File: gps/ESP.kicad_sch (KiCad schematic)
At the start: 23 parts, among them J12 ENC+RGB, J13 ENC+RGB, J7 USB_B_Micro, J9 USB_pads, SW1 RotaryEncoder_Switch, U11 SN74LV1T34DBVRG4, U3 DFR0654, U9 TCA39306DDFR

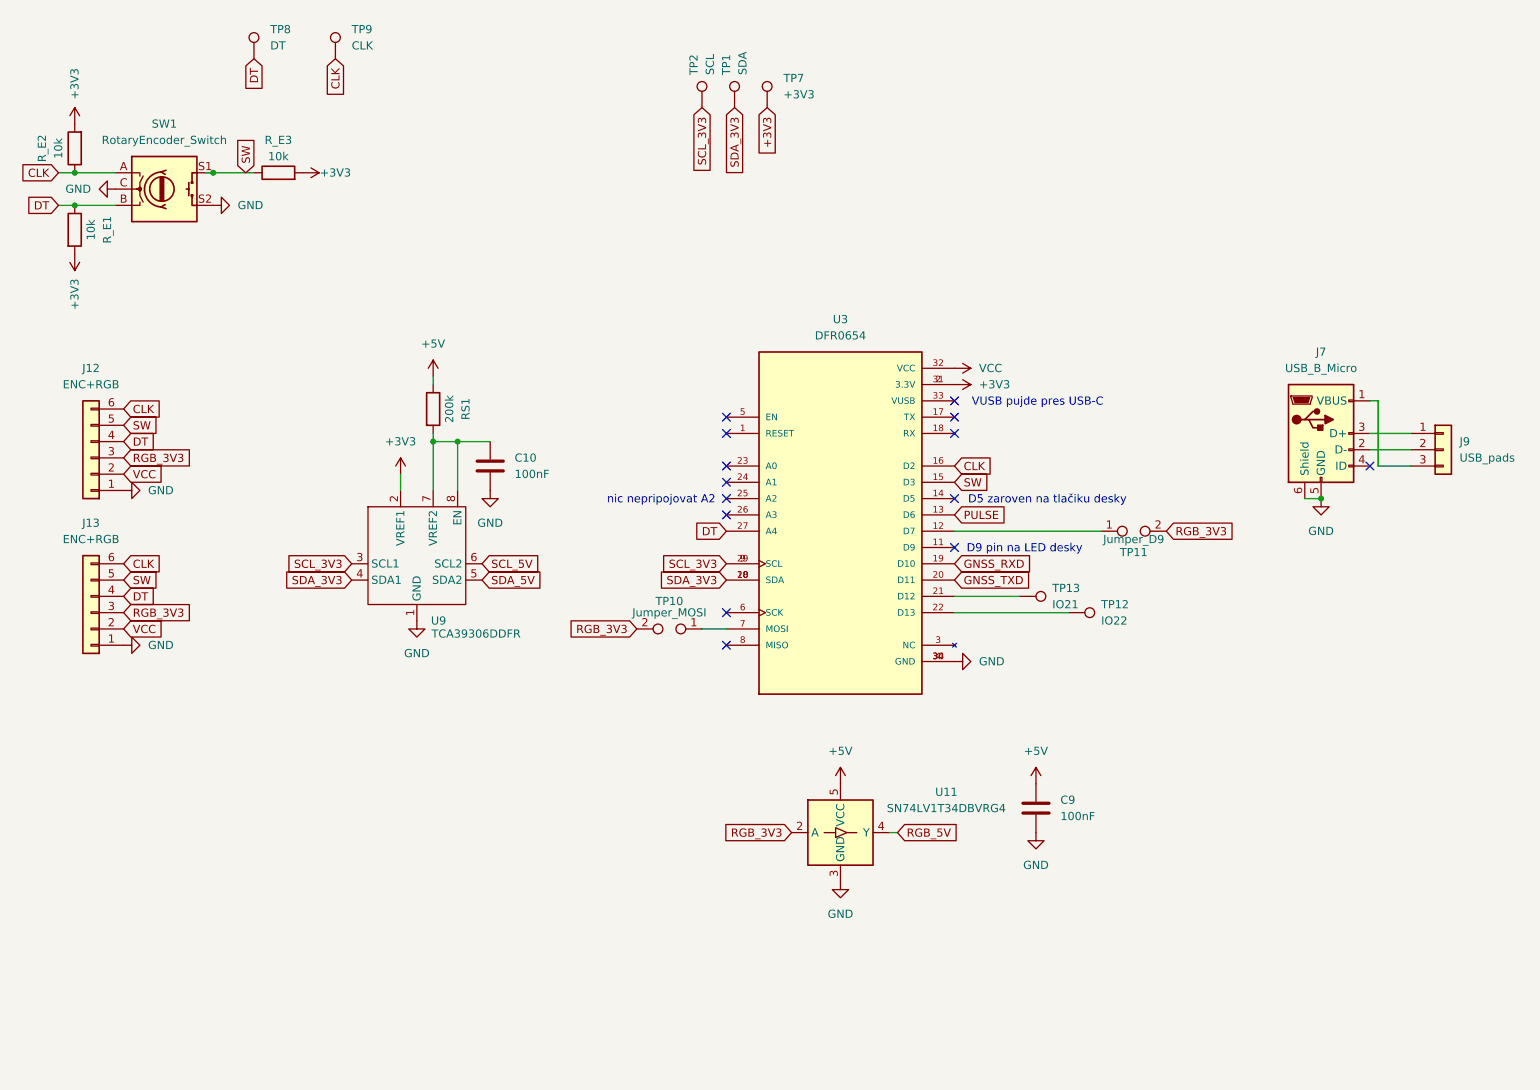
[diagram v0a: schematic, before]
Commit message: added pullup for 3V3 i2c
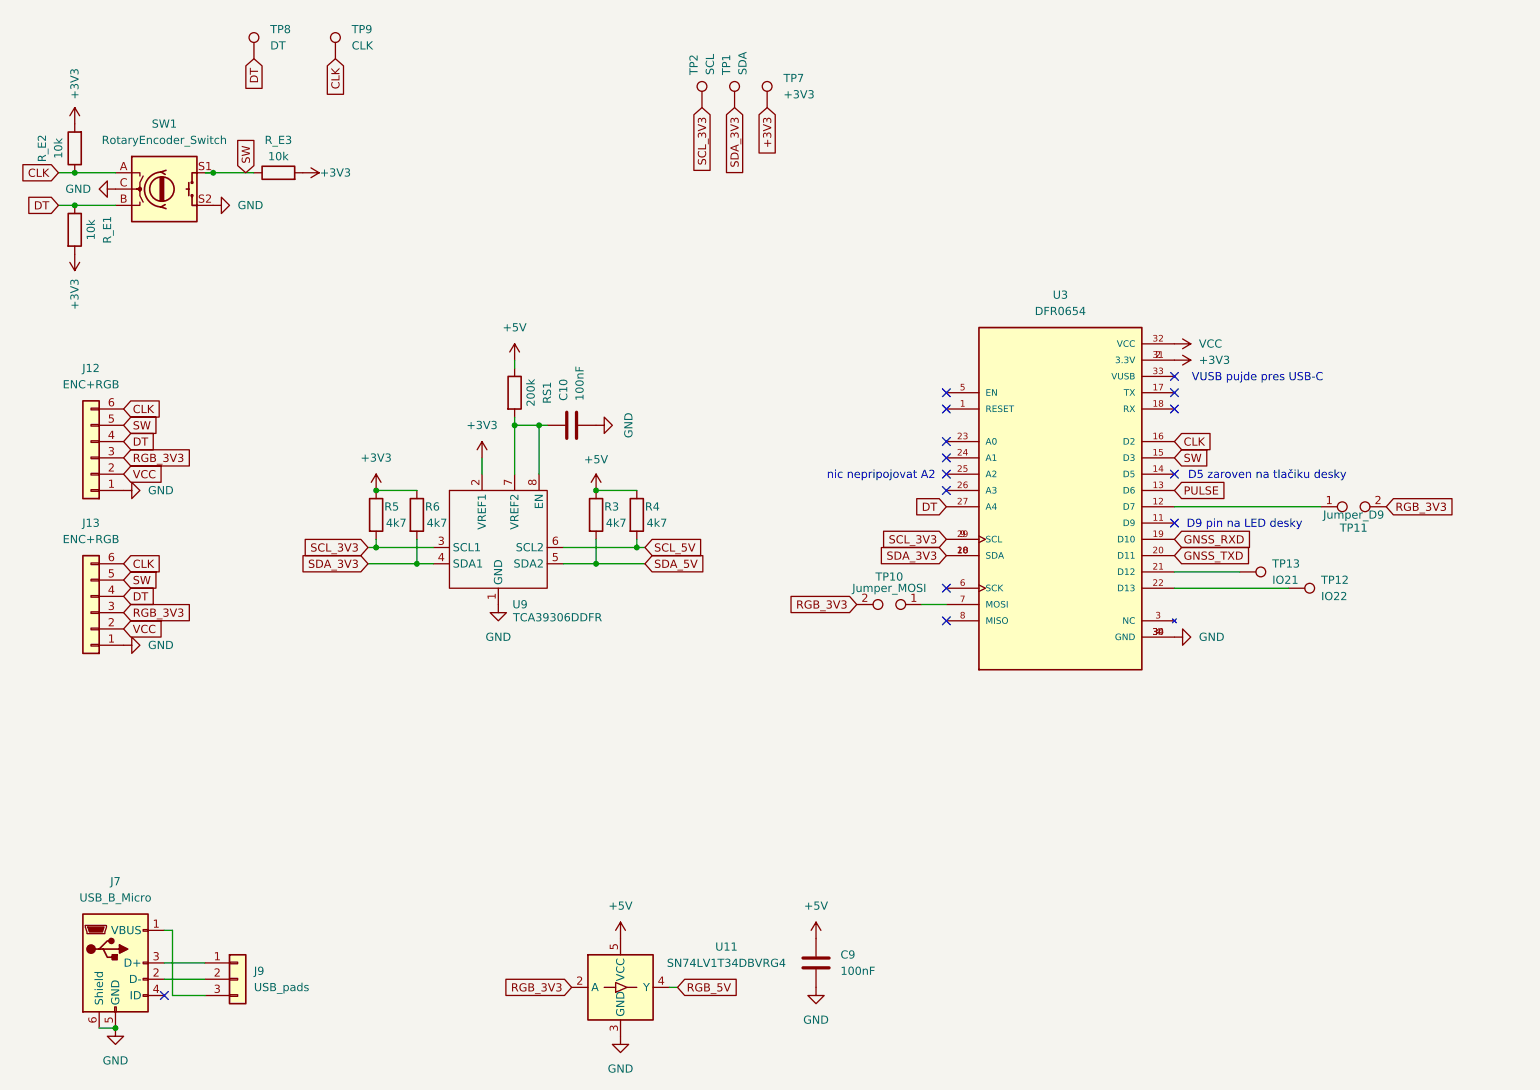
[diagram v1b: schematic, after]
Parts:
- added R3, R4, R5, R6: 4k7, Resistor_SMD:R_0805_2012Metric_Pad1.20x1.40mm_HandSolder, symbol Device:R
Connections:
- net +3V3: now also R5.1, R6.1
- net +5V: now also R3.1, R4.1
- net SCL_3V3: now also R5.2
- net SCL_5V: now also R4.2
- net SDA_3V3: now also R6.2
- net SDA_5V: now also R3.2
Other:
- moved on the sheet: C10, C9, J7, J9, RS1, TP10, TP11, TP12, TP13, U11, U3, U9

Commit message: added gerbers
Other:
- moved on the sheet: C10, R_E3, TP8, TP9
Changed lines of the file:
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@@
 	)
 	(junction
-		(at 55.88 43.18)
-		(diameter 0)
-		(color 0 0 0 0)
-	)
-	(junction
 		(at 121.92 101.6)
 		(diameter 0)
@@
 		(color 0 0 0 0)
 	)
+	(junction
+		(at 64.77 43.18)
+		(diameter 0)
+		(color 0 0 0 0)
+	)
 	(no_connect
 		(at 205.74 90.17)
@@
 	(wire
 		(pts
-			(xy 87.63 100.33) (xy 87.63 104.14)
+			(xy 67.31 43.18) (xy 64.77 43.18)
 		)
 		(stroke
@@
 	(wire
 		(pts
-			(xy 102.87 82.55) (xy 102.87 90.17)
+			(xy 87.63 100.33) (xy 87.63 104.14)
 		)
 		(stroke
@@
 	(wire
 		(pts
-			(xy 54.61 43.18) (xy 55.88 43.18)
+			(xy 102.87 82.55) (xy 102.87 90.17)
 		)
 		(stroke
@@
 	(wire
 		(pts
-			(xy 107.95 82.55) (xy 106.68 82.55)
+			(xy 110.49 82.55) (xy 106.68 82.55)
 		)
 		(stroke
@@
 	(wire
 		(pts
-			(xy 55.88 43.18) (xy 62.23 43.18)
-		)
-		(stroke
-			(width 0)
-			(type default)
-		)
-	)
-	(wire
-		(pts
 			(xy 80.01 104.14) (xy 87.63 104.14)
 		)
@@
 	(wire
 		(pts
+			(xy 64.77 43.18) (xy 55.88 43.18)
+		)
+		(stroke
+			(width 0)
+			(type default)
+		)
+	)
+	(wire
+		(pts
 			(xy 34.29 43.18) (xy 40.64 43.18)
 		)
@@
 	(global_label "DT"
 		(shape input)
-		(at 62.23 25.4 270)
+		(at 73.66 24.13 270)
 		(fields_autoplaced yes)
 		(effects
@@
 		)
 		(property "Intersheetrefs" "${INTERSHEET_REFS}"
-			(at 62.23 30.6228 90)
+			(at 73.66 29.3528 90)
 			(effects
 				(font
@@
 	(global_label "SW"
 		(shape input)
-		(at 60.96 43.18 90)
+		(at 67.31 43.18 0)
 		(fields_autoplaced yes)
 		(effects
@@
 		)
 		(property "Intersheetrefs" "${INTERSHEET_REFS}"
-			(at 60.96 37.5339 90)
+			(at 72.9561 43.18 0)
 			(effects
 				(font
@@
 	(global_label "CLK"
 		(shape input)
-		(at 74.93 25.4 270)
+		(at 86.36 24.13 270)
 		(fields_autoplaced yes)
 		(effects
@@
 		)
 		(property "Intersheetrefs" "${INTERSHEET_REFS}"
-			(at 74.93 31.9533 90)
+			(at 86.36 30.6833 90)
 			(effects
 				(font
@@
 	(symbol
 		(lib_id "Device:C")
-		(at 111.76 82.55 270)
+		(at 114.3 82.55 270)
 		(unit 1)
 		(exclude_from_sim no)
@@
 		(fields_autoplaced yes)
 		(property "Reference" "C10"
-			(at 110.4899 78.74 0)
+			(at 113.0299 78.74 0)
 			(effects
 				(font
@@
 		)
 		(property "Value" "100nF"
-			(at 113.0299 78.74 0)
+			(at 115.5699 78.74 0)
 			(effects
 				(font
@@
 		)
 		(property "Footprint" "Capacitor_SMD:C_0805_2012Metric_Pad1.18x1.45mm_HandSolder"
-			(at 107.95 83.5152 0)
+			(at 110.49 83.5152 0)
 			(effects
 				(font
@@
 		)
 		(property "Datasheet" "~"
-			(at 111.76 82.55 0)
+			(at 114.3 82.55 0)
 			(effects
 				(font
@@
 		)
 		(property "Description" "Unpolarized capacitor"
-			(at 111.76 82.55 0)
+			(at 114.3 82.55 0)
 			(effects
 				(font
@@
 	(symbol
 		(lib_id "Device:R")
-		(at 66.04 43.18 90)
+		(at 64.77 39.37 180)
 		(unit 1)
 		(exclude_from_sim no)
@@
 		(dnp no)
 		(property "Reference" "R_E3"
-			(at 66.04 38.1 90)
+			(at 59.69 39.37 90)
 			(effects
 				(font
@@
 		)
 		(property "Value" "10k"
-			(at 66.04 40.64 90)
+			(at 62.23 39.37 90)
 			(effects
 				(font
@@
 		)
 		(property "Footprint" "Resistor_SMD:R_0805_2012Metric_Pad1.20x1.40mm_HandSolder"
-			(at 66.04 44.958 90)
+			(at 66.548 39.37 90)
 			(effects
 				(font
@@
 		)
 		(property "Datasheet" "~"
-			(at 66.04 43.18 0)
+			(at 64.77 39.37 0)
 			(effects
 				(font
@@
 		)
 		(property "Description" "Resistor"
-			(at 66.04 43.18 0)
+			(at 64.77 39.37 0)
 			(effects
 				(font
@@
 	(symbol
 		(lib_id "power:GND")
-		(at 115.57 82.55 90)
+		(at 118.11 82.55 90)
 		(unit 1)
 		(exclude_from_sim no)
@@
 		(fields_autoplaced yes)
 		(property "Reference" "#PWR059"
-			(at 121.92 82.55 0)
+			(at 124.46 82.55 0)
 			(effects
 				(font
@@
 		)
 		(property "Value" "GND"
-			(at 120.65 82.55 0)
+			(at 123.19 82.55 0)
 			(effects
 				(font
@@
 		)
 		(property "Footprint" ""
-			(at 115.57 82.55 0)
+			(at 118.11 82.55 0)
 			(effects
 				(font
@@
 		)
 		(property "Datasheet" ""
-			(at 115.57 82.55 0)
+			(at 118.11 82.55 0)
 			(effects
 				(font
@@
 		)
 		(property "Description" "Power symbol creates a global label with name \"GND\" , ground"
-			(at 115.57 82.55 0)
+			(at 118.11 82.55 0)
 			(effects
 				(font
@@
 	(symbol
 		(lib_id "power:+3V3")
-		(at 69.85 43.18 270)
+		(at 64.77 35.56 0)
 		(unit 1)
 		(exclude_from_sim no)
@@
 		(dnp no)
 		(property "Reference" "#PWR027"
-			(at 66.04 43.18 0)
+			(at 64.77 39.37 0)
 			(effects
 				(font
@@
 		)
 		(property "Value" "+3V3"
-			(at 74.93 43.18 90)
+			(at 64.77 30.48 90)
 			(effects
 				(font
@@
 		)
 		(property "Footprint" ""
-			(at 69.85 43.18 0)
+			(at 64.77 35.56 0)
 			(effects
 				(font
@@
 		)
 		(property "Datasheet" ""
-			(at 69.85 43.18 0)
+			(at 64.77 35.56 0)
 			(effects
 				(font
@@
 		)
 		(property "Description" "Power symbol creates a global label with name \"+3V3\""
-			(at 69.85 43.18 0)
+			(at 64.77 35.56 0)
 			(effects
 				(font
@@
 	(symbol
 		(lib_id "Connector:TestPoint")
-		(at 62.23 25.4 0)
+		(at 73.66 24.13 0)
 		(unit 1)
 		(exclude_from_sim no)
@@
 		(fields_autoplaced yes)
 		(property "Reference" "TP8"
-			(at 64.77 20.8279 0)
+			(at 76.2 19.5579 0)
 			(effects
 				(font
@@
 		)
 		(property "Value" "DT"
-			(at 64.77 23.3679 0)
+			(at 76.2 22.0979 0)
 			(effects
 				(font
@@
 		)
 		(property "Footprint" "TestPoint:TestPoint_Loop_D1.80mm_Drill1.0mm_Beaded"
-			(at 67.31 25.4 0)
+			(at 78.74 24.13 0)
 			(effects
 				(font
@@
 		)
 		(property "Datasheet" "~"
-			(at 67.31 25.4 0)
+			(at 78.74 24.13 0)
 			(effects
 				(font
@@
 		)
 		(property "Description" "test point"
-			(at 62.23 25.4 0)
+			(at 73.66 24.13 0)
 			(effects
 				(font
@@
 	(symbol
 		(lib_id "Connector:TestPoint")
-		(at 74.93 25.4 0)
+		(at 86.36 24.13 0)
 		(unit 1)
 		(exclude_from_sim no)
@@
 		(fields_autoplaced yes)
 		(property "Reference" "TP9"
-			(at 77.47 20.8279 0)
+			(at 88.9 19.5579 0)
 			(effects
 				(font
@@
 		)
 		(property "Value" "CLK"
-			(at 77.47 23.3679 0)
+			(at 88.9 22.0979 0)
 			(effects
 				(font
@@
 		)
 		(property "Footprint" "TestPoint:TestPoint_Loop_D1.80mm_Drill1.0mm_Beaded"
-			(at 80.01 25.4 0)
+			(at 91.44 24.13 0)
 			(effects
 				(font
@@
 		)
 		(property "Datasheet" "~"
-			(at 80.01 25.4 0)
+			(at 91.44 24.13 0)
 			(effects
 				(font
@@
 		)
 		(property "Description" "test point"
-			(at 74.93 25.4 0)
+			(at 86.36 24.13 0)
 			(effects
 				(font

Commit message: cleaned schematic
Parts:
- removed C10, C9: 100nF, Capacitor_SMD:C_0805_2012Metric_Pad1.18x1.45mm_HandSolder, symbol Device:C
- removed J12: ENC+RGB, Connector_PinSocket_2.54mm:PinSocket_1x06_P2.54mm_Vertical, symbol Connector_Generic:Conn_01x06
- removed J13: ENC+RGB, Connector_PinHeader_2.54mm:PinHeader_1x06_P2.54mm_Vertical, symbol Connector_Generic:Conn_01x06
- removed J7: USB_B_Micro, KiCad:USB3145301A, symbol Connector:USB_B_Micro
- removed J9: USB_pads, Connector_PinSocket_2.54mm:PinSocket_1x03_P2.54mm_Vertical, symbol Connector_Generic:Conn_01x03
- removed R3, R4, R5, R6: 4k7, Resistor_SMD:R_0805_2012Metric_Pad1.20x1.40mm_HandSolder, symbol Device:R
- removed RS1: 200k, Resistor_SMD:R_0805_2012Metric_Pad1.20x1.40mm_HandSolder, symbol Device:R
- removed R_E1, R_E2, R_E3: 10k, Resistor_SMD:R_0805_2012Metric_Pad1.20x1.40mm_HandSolder, symbol Device:R
- removed SW1: RotaryEncoder_Switch, Rotary_Encoder:RotaryEncoder_20mm_WO_mount_holes, symbol Device:RotaryEncoder_Switch
- removed TP1: SDA, TestPoint:TestPoint_Loop_D1.80mm_Drill1.0mm_Beaded, symbol Connector:TestPoint
- removed TP10: Jumper_MOSI, Resistor_SMD:R_0805_2012Metric_Pad1.20x1.40mm_HandSolder, symbol Connector:TestPoint_2Pole
- removed TP11: Jumper_D9, Resistor_SMD:R_0805_2012Metric_Pad1.20x1.40mm_HandSolder, symbol Connector:TestPoint_2Pole
- removed TP12: IO22, TestPoint:TestPoint_Loop_D1.80mm_Drill1.0mm_Beaded, symbol Connector:TestPoint
- removed TP13: IO21, TestPoint:TestPoint_Loop_D1.80mm_Drill1.0mm_Beaded, symbol Connector:TestPoint
- removed TP2: SCL, TestPoint:TestPoint_Loop_D1.80mm_Drill1.0mm_Beaded, symbol Connector:TestPoint
- removed TP7: +3V3, TestPoint:TestPoint_Loop_D1.80mm_Drill1.0mm_Beaded, symbol Connector:TestPoint
- removed TP8: DT, TestPoint:TestPoint_Loop_D1.80mm_Drill1.0mm_Beaded, symbol Connector:TestPoint
- removed TP9: CLK, TestPoint:TestPoint_Loop_D1.80mm_Drill1.0mm_Beaded, symbol Connector:TestPoint
- removed U11: SN74LV1T34DBVRG4, Package_TO_SOT_SMD:SOT-23-5, symbol Logic_LevelTranslator:SN74LV1T34DBV
- removed U3: DFR0654, DFR0654:DFR0654_2, symbol DFR0654:DFR0654
- removed U9: TCA39306DDFR, Package_TO_SOT_SMD:SOT-23-8, symbol shifter:TCA39306DCURQ1
- added AE1: Antenna_Shield, w_conn_rf:lemo_epb00250ntn, symbol Device:Antenna_Shield
- added C1: 10uF, Capacitor_Tantalum_SMD:CP_EIA-3528-15_AVX-H_Pad1.50x2.35mm_HandSolder, symbol Device:C_Polarized
- added C2: 1uF, Capacitor_SMD:C_0603_1608Metric_Pad1.08x0.95mm_HandSolder, symbol Device:C
- added C3: 10n, Capacitor_SMD:C_0805_2012Metric_Pad1.18x1.45mm_HandSolder, symbol Device:C
- added J3: USB_pads, Connector_PinHeader_2.54mm:PinHeader_1x04_P2.54mm_Vertical, symbol Connector_Generic:Conn_01x04
- added L1: 27nH, Inductor_SMD:L_0402_1005Metric_Pad0.77x0.64mm_HandSolder, symbol Device:L
- added R2: 10, Resistor_SMD:R_1206_3216Metric_Pad1.30x1.75mm_HandSolder, symbol Device:R
- added TP4: GNSS_TXD, TestPoint:TestPoint_Loop_D1.80mm_Drill1.0mm_Beaded, symbol Connector:TestPoint
- added TP5: GNSS_RXD, TestPoint:TestPoint_Loop_D1.80mm_Drill1.0mm_Beaded, symbol Connector:TestPoint
- added U1: NEO-M9N, RF_GPS:ublox_NEO, symbol RF_GPS:NEO-M8N
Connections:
- net +3V3: now also C1.1, C2.1, U1.22 (V_BCKP), U1.23 (VCC)
- net GND: now also AE1.2 (Shield), C1.2, C2.2, C3.1, J3.1 (Pin_1), U1.10 (GND), U1.12 (GND), U1.13 (GND), U1.24 (GND)
- net GNSS_RXD: now also TP5.1, U1.21 (RXD/SPI_MOSI)
- net GNSS_TXD: now also TP4.1, U1.20 (TXD/SPI_MISO)
- net PULSE: now also U1.3 (TIMEPULSE)
- new net: J3.2 (Pin_2), U1.1 (~{SAFEBOOT})
- new net: J3.3 (Pin_3), U1.5 (USB_DM)
- new net: J3.4 (Pin_4), U1.6 (USB_DP)
- new net: AE1.1 (A), L1.1, U1.11 (RF_IN)
- new net: C3.2, L1.2, R2.2
- new net: R2.1, U1.9 (VCC_RF)
- no-connect marks 14 -> 7
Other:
- note removed: "D5 zaroven na tlačiku desky"
- note removed: "D9 pin na LED desky"
- note removed: "VUSB pujde pres USB-C"
- note removed: "nic nepripojovat A2"

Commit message: updated pdf/
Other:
- title: (none) -> GNSS_Geret
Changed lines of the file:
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@@
 	(generator_version "8.0")
 	(paper "A4")
+	(title_block
+		(title "GNSS_Geret")
+		(rev "1")
+	)
 	(junction
 		(at 191.77 105.41)
